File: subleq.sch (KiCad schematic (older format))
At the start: 0 parts

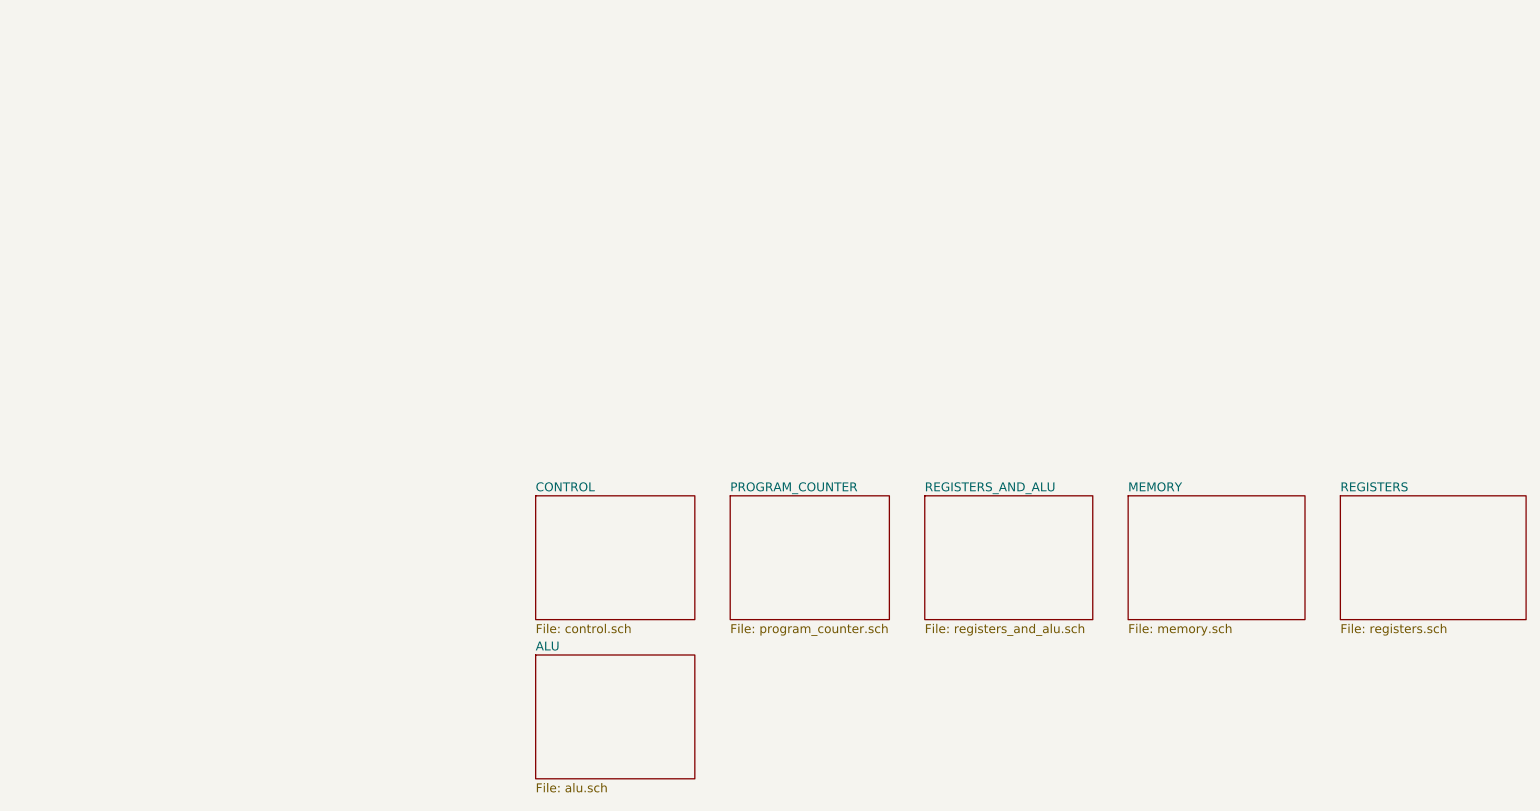
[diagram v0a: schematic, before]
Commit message: split alu regs complete
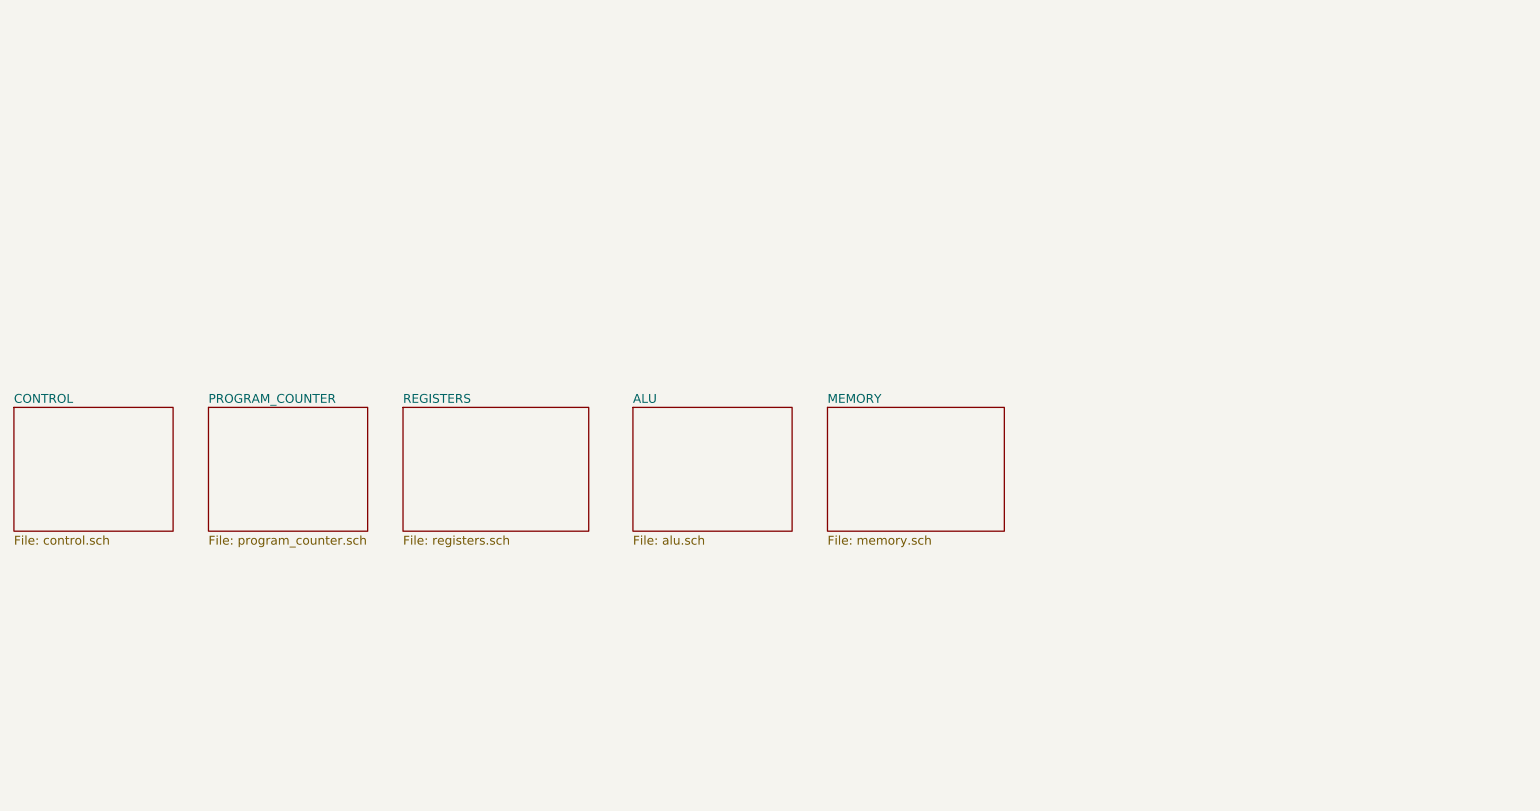
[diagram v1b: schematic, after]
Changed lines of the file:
@@
 $Descr USLedger 17000 11000
 encoding utf-8
-Sheet 1 7
+Sheet 1 6
 Title ""
 Date ""
@@
 $EndDescr
 $Sheet
-S 10100 6200 900  700
+S 7150 5700 900  700
 U 5C4E38C4
 F0 "CONTROL" 50
@@
 $EndSheet
 $Sheet
-S 11200 6200 900  700
+S 8250 5700 900  700
 U 5C4F5C3F
 F0 "PROGRAM_COUNTER" 50
@@
 $EndSheet
 $Sheet
-S 12300 6200 950  700
-U 5CB820A3
-F0 "REGISTERS_AND_ALU" 50
-F1 "registers_and_alu.sch" 50
-$EndSheet
-$Sheet
-S 13450 6200 1000 700
+S 11750 5700 1000 700
 U 5CBABD04
 F0 "MEMORY" 50
@@
 $EndSheet
 $Sheet
-S 14650 6200 1050 700
+S 9350 5700 1050 700
 U 5CBC693B
 F0 "REGISTERS" 50
@@
 $EndSheet
 $Sheet
-S 10100 7100 900  700
+S 10650 5700 900  700
 U 5C4D52FD
 F0 "ALU" 50

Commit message: done for the night passing drc
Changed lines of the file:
@@
 $Descr USLedger 17000 11000
 encoding utf-8
-Sheet 1 6
+Sheet 1 7
 Title ""
 Date ""
@@
 F1 "alu.sch" 50
 $EndSheet
+$Sheet
+S 12950 5700 900  700
+U 5C692EB5
+F0 "SUPPORT" 50
+F1 "support.sch" 50
+$EndSheet
+$Comp
+L power:VCC #PWR01
+U 1 1 5C69AC68
+P 12050 3700
+F 0 "#PWR01" H 12050 3550 50  0001 C CNN
+F 1 "VCC" H 12067 3873 50  0000 C CNN
+F 2 "" H 12050 3700 50  0001 C CNN
+F 3 "" H 12050 3700 50  0001 C CNN
+	1    12050 3700
+	1    0    0    -1
+$EndComp
+$Comp
+L power:GND #PWR02
+U 1 1 5C69AC91
+P 12050 4400
+F 0 "#PWR02" H 12050 4150 50  0001 C CNN
+F 1 "GND" H 12055 4227 50  0000 C CNN
+F 2 "" H 12050 4400 50  0001 C CNN
+F 3 "" H 12050 4400 50  0001 C CNN
+	1    12050 4400
+	1    0    0    -1
+$EndComp
+$Comp
+L power:PWR_FLAG #FLG01
+U 1 1 5C69B2A8
+P 12050 3800
+F 0 "#FLG01" H 12050 3875 50  0001 C CNN
+F 1 "PWR_FLAG" H 12050 3973 50  0000 C CNN
+F 2 "" H 12050 3800 50  0001 C CNN
+F 3 "~" H 12050 3800 50  0001 C CNN
+	1    12050 3800
+	-1   0    0    1
+$EndComp
+$Comp
+L power:PWR_FLAG #FLG02
+U 1 1 5C69B2BA
+P 12050 4300
+F 0 "#FLG02" H 12050 4375 50  0001 C CNN
+F 1 "PWR_FLAG" H 12050 4474 50  0000 C CNN
+F 2 "" H 12050 4300 50  0001 C CNN
+F 3 "~" H 12050 4300 50  0001 C CNN
+	1    12050 4300
+	1    0    0    -1
+$EndComp
+Wire Wire Line
+	12050 3800 12050 3700
+Wire Wire Line
+	12050 4300 12050 4400
 $EndSCHEMATC
